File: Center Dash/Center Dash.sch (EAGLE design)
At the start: 90 parts, among them J1 502585-0470, Q1 BSS138, Q2 BSS138, Q3 BSS138, Q4 BSS138, U1 ADG3304BRUZ-REEL7, U2 TPS54540DDARQ1

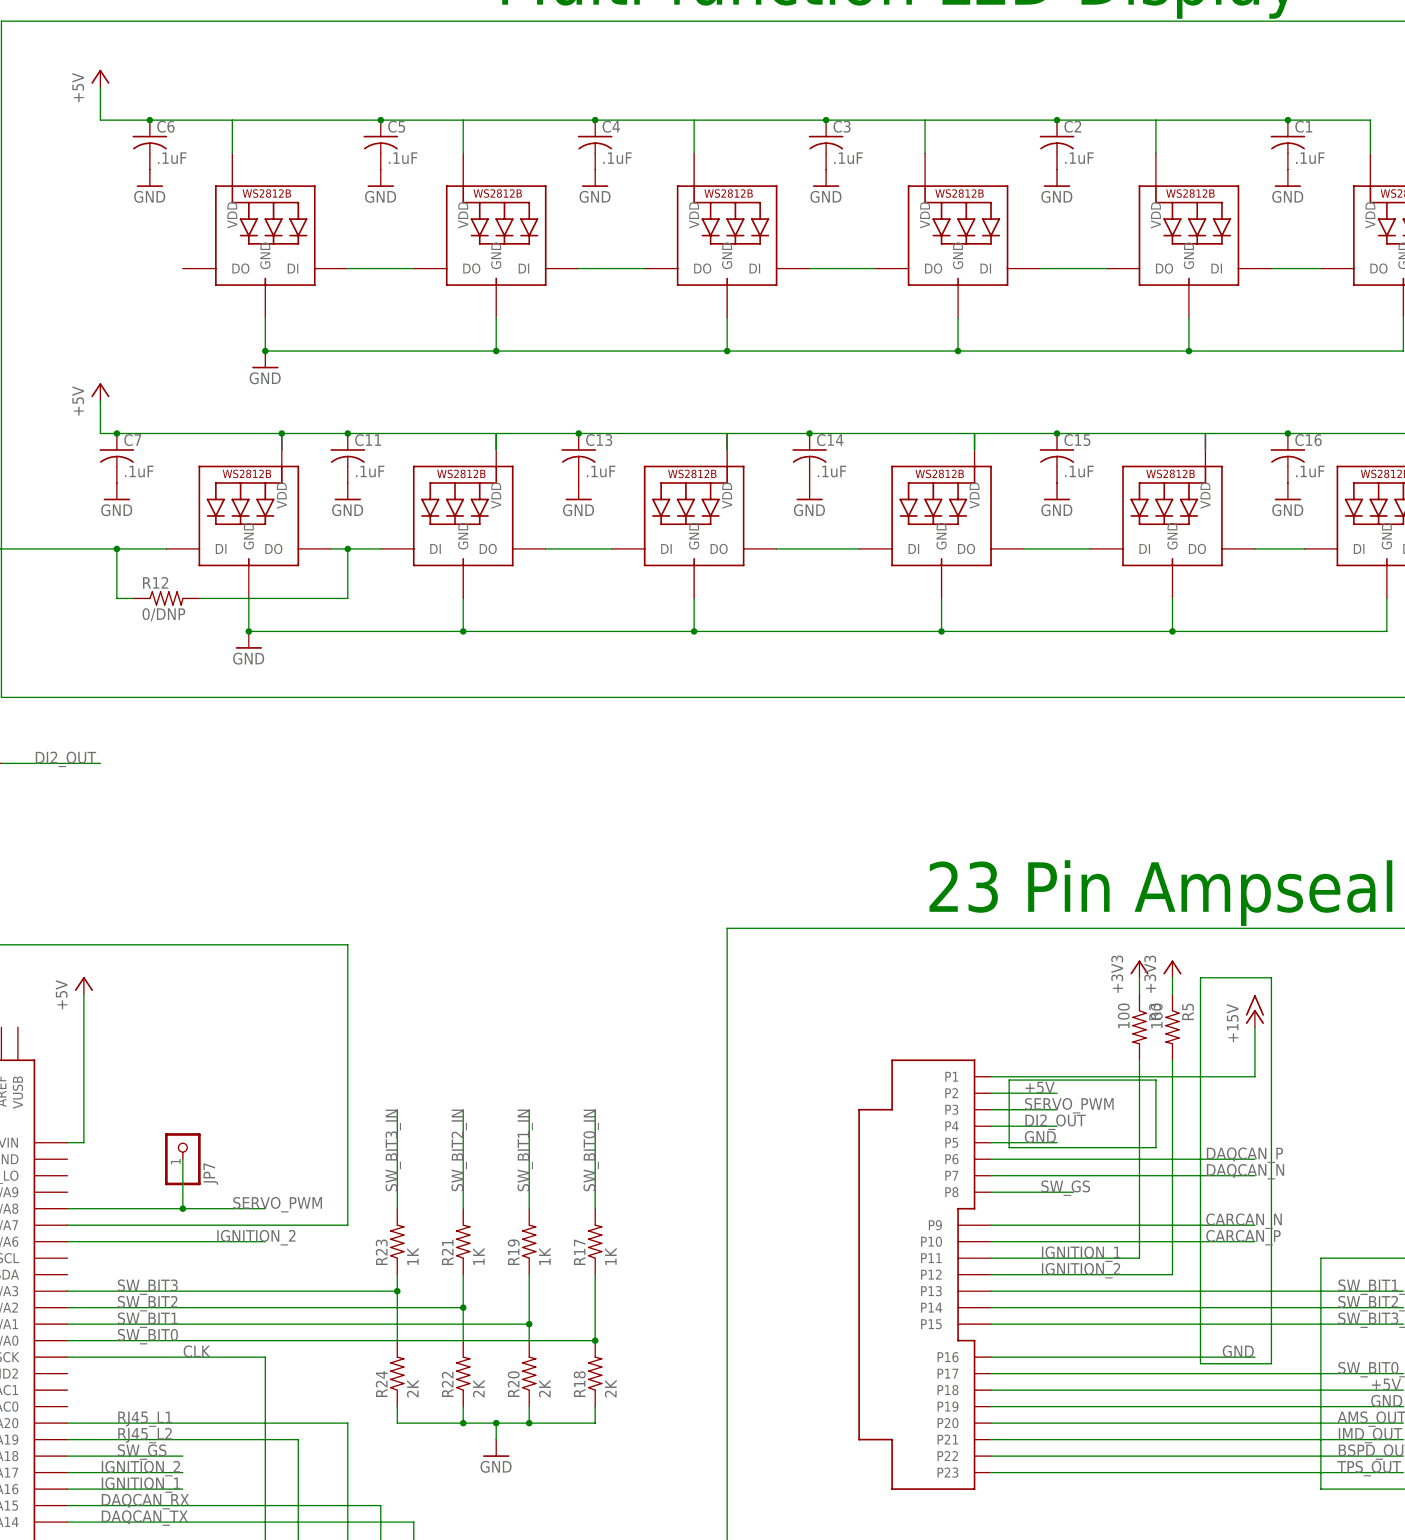
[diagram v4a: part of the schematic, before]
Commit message: Fixed two of the via overlaps
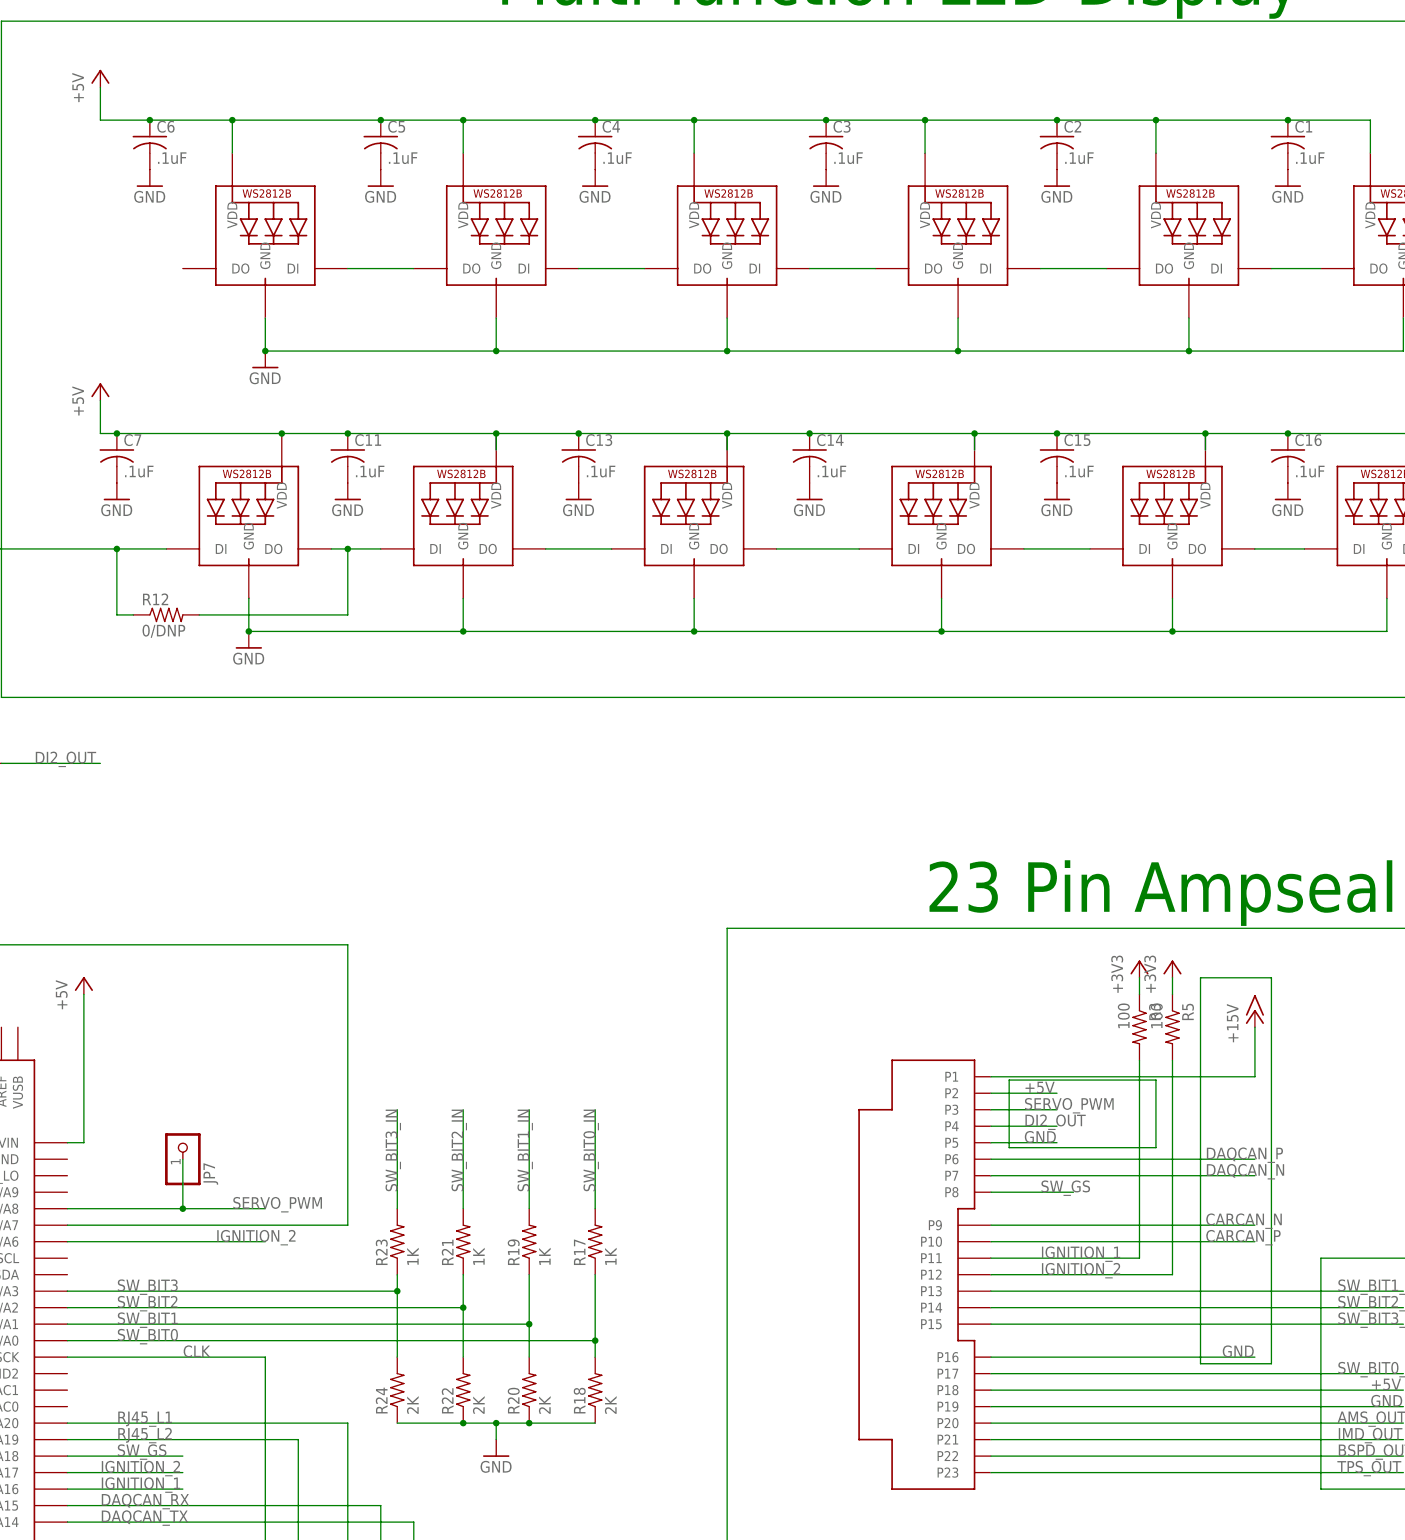
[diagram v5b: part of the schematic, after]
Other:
- moved on the sheet: R12, R18, R20, R22, R24
